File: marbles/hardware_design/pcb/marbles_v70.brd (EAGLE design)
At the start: 88.9 x 106 mm, 213 parts, among them IC1 R-78E3.3-0.5, IC10 TL074PW, IC2 STM32F405RGT6, IC3 LD2981ABU33, IC4 DAC8164ICPW, IC5 MCP6004, IC6 MCP6004, IC7 OPA4171, IC8 LM4040B10, IC9 LM324PW, J1 PJ301_THONKICONN6, J10 PJ301_THONKICONN6, J11 PJ301_THONKICONN6, J12 PJ301_THONKICONN6, J13 PJ301_THONKICONN6, J14 PJ301_THONKICONN6, J15 PJ301_THONKICONN6, J16 PJ301_THONKICONN6, J2 PJ301_THONKICONN6, J3 PJ301_THONKICONN6, J4 PJ301_THONKICONN6, J5 PJ301_THONKICONN6, J6 PJ301_THONKICONN6, J7 PJ301_THONKICONN6, J8 PJ301_THONKICONN6, J9 PJ301_THONKICONN6, Q1 8MHz, Q2 MMBT3904, Q3 MMBT3904, SW1 LP4OA1PBCT, SW2 LP4OA1PBCT

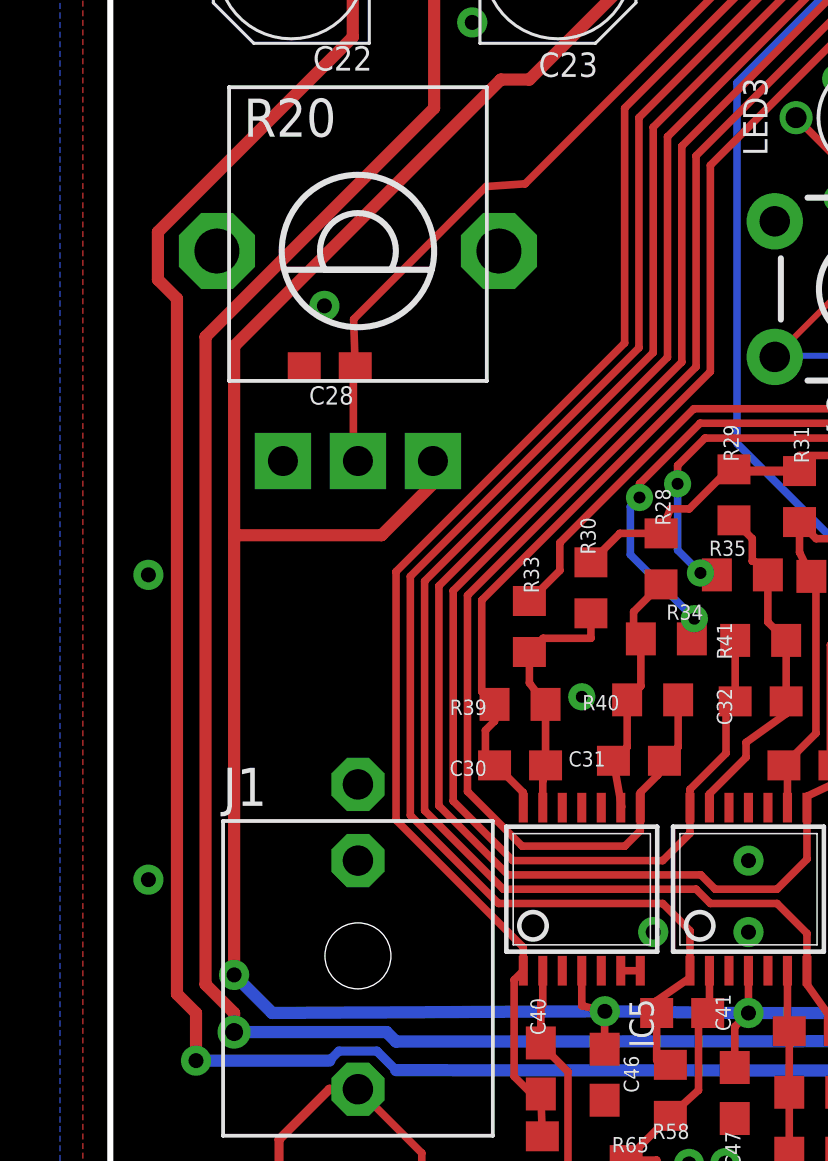
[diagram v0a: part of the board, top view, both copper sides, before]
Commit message: Fixed Collision of c28 with POT, tested ok.
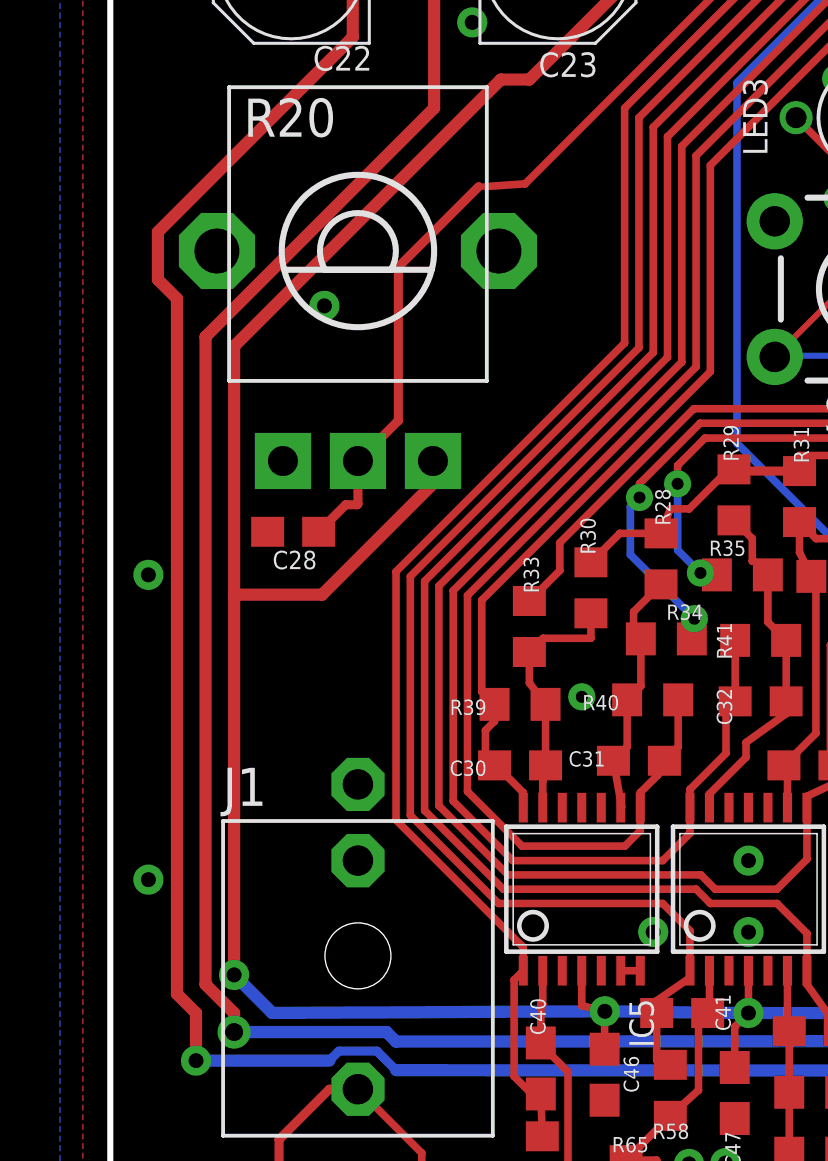
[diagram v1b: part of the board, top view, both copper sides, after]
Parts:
- moved C28 5.62 mm to (6.10, 49.7)
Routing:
- net ADC_T_BIAS_POT: track 56.9 -> 60.0 mm
- net +3V3_A: track 313.9 -> 314.7 mm
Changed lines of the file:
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@@
 <?xml version="1.0" encoding="utf-8"?>
 <!DOCTYPE eagle SYSTEM "eagle.dtd">
-<eagle version="9.5.2">
+<eagle version="9.6.1">
 <drawing>
 <settings>
@@
 <layer number="37" name="tTest" color="7" fill="1" visible="no" active="yes"/>
 <layer number="38" name="bTest" color="7" fill="1" visible="no" active="yes"/>
-<layer number="39" name="tKeepout" color="4" fill="11" visible="yes" active="yes"/>
-<layer number="40" name="bKeepout" color="1" fill="11" visible="yes" active="yes"/>
-<layer number="41" name="tRestrict" color="4" fill="10" visible="yes" active="yes"/>
-<layer number="42" name="bRestrict" color="1" fill="10" visible="yes" active="yes"/>
+<layer number="39" name="tKeepout" color="4" fill="11" visible="no" active="yes"/>
+<layer number="40" name="bKeepout" color="1" fill="11" visible="no" active="yes"/>
+<layer number="41" name="tRestrict" color="4" fill="10" visible="no" active="yes"/>
+<layer number="42" name="bRestrict" color="1" fill="10" visible="no" active="yes"/>
 <layer number="43" name="vRestrict" color="2" fill="10" visible="no" active="yes"/>
 <layer number="44" name="Drills" color="7" fill="1" visible="no" active="yes"/>
 <layer number="45" name="Holes" color="7" fill="1" visible="no" active="yes"/>
-<layer number="46" name="Milling" color="3" fill="1" visible="no" active="yes"/>
+<layer number="46" name="Milling" color="3" fill="1" visible="yes" active="yes"/>
 <layer number="47" name="Measures" color="7" fill="1" visible="no" active="yes"/>
 <layer number="48" name="Document" color="7" fill="1" visible="yes" active="yes"/>
@@
 <attribute name="VALUE" x="36.722" y="60.833" size="0.6096" layer="27" rot="R90"/>
 </element>
-<element name="C28" library="rcl" package="C0603" value="100n" x="7.3152" y="55.1815" smashed="yes" rot="R180">
-<attribute name="NAME" x="8.1089" y="54.5465" size="0.6096" layer="25" rot="R180"/>
-<attribute name="VALUE" x="8.109" y="53.9115" size="0.4064" layer="27" rot="R180"/>
+<element name="C28" library="rcl" package="C0603" value="100n" x="6.096" y="49.6951" smashed="yes" rot="R180">
+<attribute name="NAME" x="6.8897" y="49.0601" size="0.6096" layer="25" rot="R180"/>
+<attribute name="VALUE" x="6.8898" y="48.4251" size="0.4064" layer="27" rot="R180"/>
 </element>
 <element name="C17" library="rcl" package="C0603" value="100n" x="20.5232" y="73.1901" smashed="yes" rot="R180">
@@
 <wire x1="47.625" y1="86.0425" x2="46.95" y2="86.7175" width="0.254" layer="16"/>
 <wire x1="46.95" y1="86.7175" x2="46.95" y2="88.25" width="0.254" layer="16"/>
-<wire x1="4.1275" y1="34.925" x2="4.1275" y2="49.5808" width="0.4064" layer="1"/>
+<wire x1="4.1275" y1="34.925" x2="4.1275" y2="47.5996" width="0.4064" layer="1"/>
 <wire x1="24.725" y1="74.255" x2="24.725" y2="75.2325" width="0.4064" layer="1"/>
-<wire x1="4.1275" y1="49.5808" x2="4.1275" y2="55.88" width="0.4064" layer="1"/>
+<wire x1="4.1275" y1="47.5996" x2="4.1275" y2="55.88" width="0.4064" layer="1"/>
 <wire x1="10.755" y1="52.055" x2="10.755" y2="51.293" width="0.4064" layer="1"/>
-<wire x1="10.755" y1="51.293" x2="9.0428" y2="49.5808" width="0.4064" layer="1"/>
-<wire x1="9.0428" y1="49.5808" x2="4.1275" y2="49.5808" width="0.4064" layer="1"/>
+<wire x1="10.755" y1="51.293" x2="7.0616" y2="47.5996" width="0.4064" layer="1"/>
+<wire x1="7.0616" y1="47.5996" x2="4.1275" y2="47.5996" width="0.4064" layer="1"/>
 <wire x1="19.05" y1="68.58" x2="24.725" y2="74.255" width="0.4064" layer="1"/>
 <wire x1="16.9725" y1="68.58" x2="19.05" y2="68.58" width="0.4064" layer="1"/>
@@
 <contactref element="C28" pad="1"/>
 <contactref element="IC2" pad="16"/>
-<wire x1="8.1652" y1="55.1815" x2="8.1026" y2="55.1189" width="0.254" layer="1"/>
-<wire x1="8.1026" y1="55.1189" x2="8.1026" y2="52.2074" width="0.254" layer="1"/>
-<wire x1="8.1026" y1="52.2074" x2="8.255" y2="52.055" width="0.254" layer="1"/>
 <wire x1="35.2425" y1="84.2963" x2="38.9192" y2="84.2963" width="0.254" layer="1"/>
 <wire x1="32.0675" y1="81.1213" x2="35.2425" y2="84.2963" width="0.254" layer="1"/>
 <wire x1="32.0675" y1="79.5337" x2="32.0675" y2="81.1213" width="0.254" layer="1"/>
 <wire x1="32.0675" y1="79.5337" x2="13.829025" y2="61.295225" width="0.254" layer="1"/>
-<wire x1="12.526540625" y1="61.204471875" x2="8.110615625" y2="56.7808" width="0.254" layer="1"/>
-<wire x1="8.1652" y1="55.1815" x2="8.110615625" y2="56.7808" width="0.254" layer="1"/>
-<wire x1="13.829025" y1="61.295225" x2="12.526540625" y2="61.204471875" width="0.254" layer="1"/>
+<wire x1="12.526540625" y1="61.204471875" x2="13.829025" y2="61.295225" width="0.254" layer="1"/>
 <wire x1="47.3075" y1="84.9313" x2="47.3701" y2="84.9939" width="0.254" layer="1"/>
 <wire x1="47.3701" y1="84.9939" x2="47.3675" y2="84.9939" width="0.254" layer="1"/>
@@
 <wire x1="43.0212" y1="85.2488" x2="43.3387" y2="84.9313" width="0.254" layer="1"/>
 <wire x1="43.3387" y1="84.9313" x2="47.3075" y2="84.9313" width="0.254" layer="1"/>
+<wire x1="6.946" y1="49.6951" x2="7.8477" y2="50.5968" width="0.3048" layer="1"/>
+<wire x1="7.8477" y1="50.5968" x2="8.2296" y2="50.5968" width="0.3048" layer="1"/>
+<wire x1="8.2296" y1="50.5968" x2="8.255" y2="50.6222" width="0.3048" layer="1"/>
+<wire x1="8.255" y1="50.6222" x2="8.255" y2="52.055" width="0.3048" layer="1"/>
+<wire x1="8.255" y1="52.055" x2="9.6012" y2="53.4012" width="0.3048" layer="1"/>
+<wire x1="9.6012" y1="53.4012" x2="9.6012" y2="58.5216" width="0.3048" layer="1"/>
+<wire x1="9.6012" y1="58.5216" x2="12.284071875" y2="61.204471875" width="0.3048" layer="1"/>
+<wire x1="12.284071875" y1="61.204471875" x2="12.526540625" y2="61.204471875" width="0.2032" layer="1"/>
 </signal>
 <signal name="SW_T_RANGE">
